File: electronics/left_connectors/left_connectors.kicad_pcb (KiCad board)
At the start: 2 copper layers, 47.5 x 41.3 mm, 0 parts

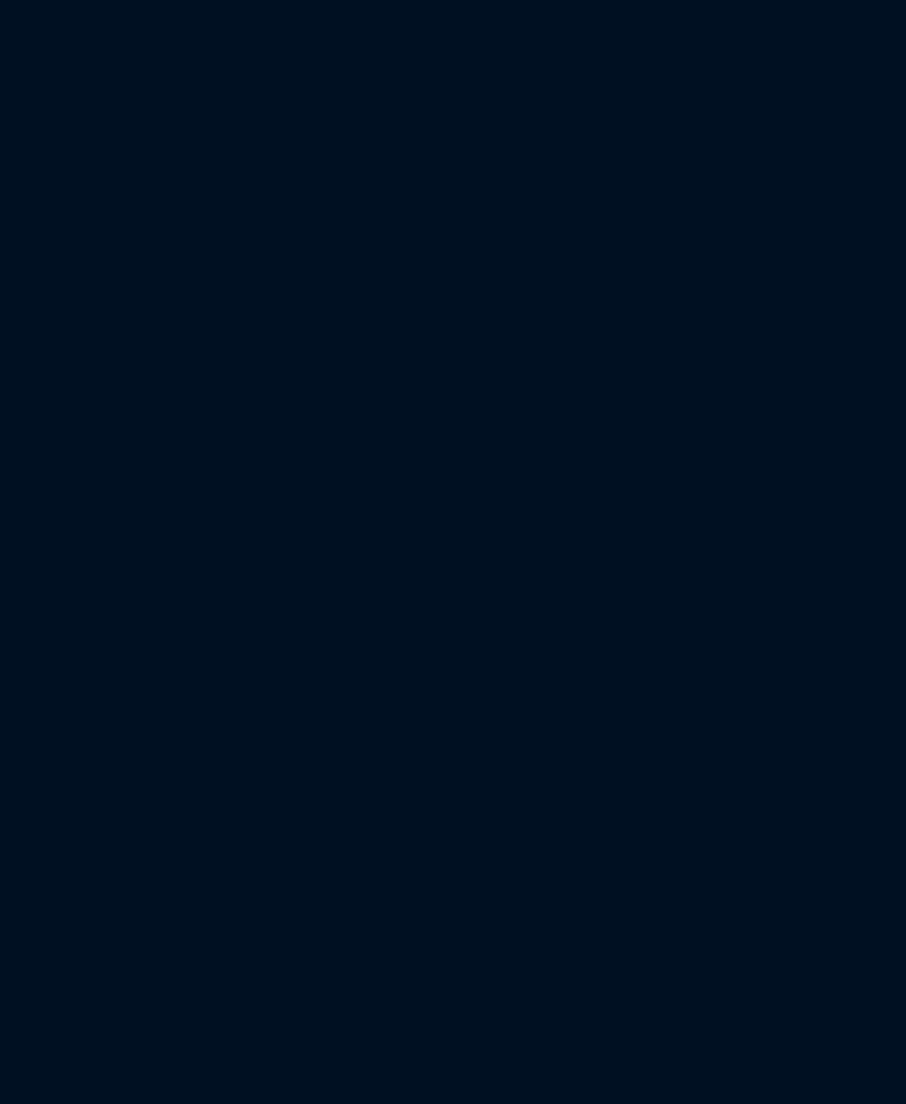
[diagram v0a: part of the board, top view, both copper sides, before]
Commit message: connectors board parts allocated
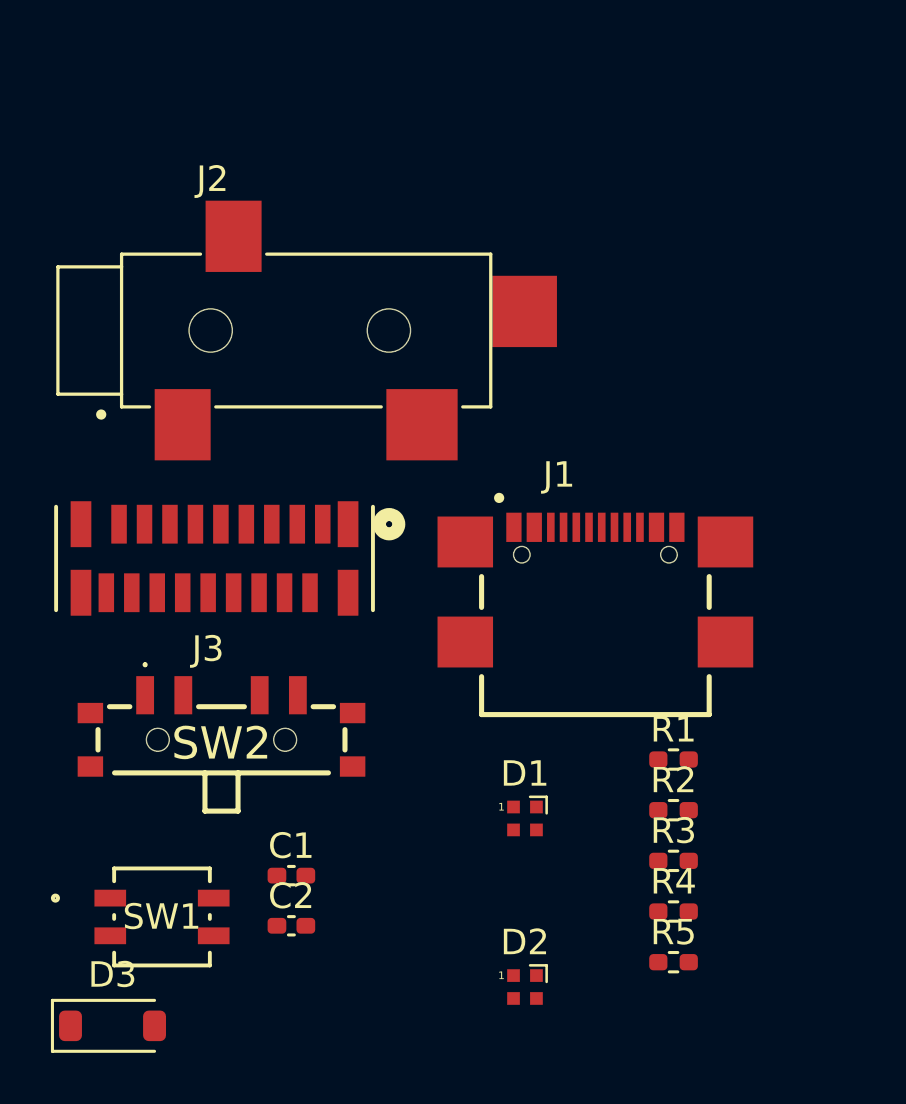
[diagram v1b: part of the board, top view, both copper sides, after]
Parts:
- added C1: 1uF, Capacitor_SMD:C_0402_1005Metric_Pad0.74x0.62mm_HandSolder, F.Cu at (100.8, 148.5)
- added C2: 1uF, Capacitor_SMD:C_0402_1005Metric_Pad0.74x0.62mm_HandSolder, F.Cu at (100.8, 150.5)
- added D1: power_led, LED_SMD:LED_SK6812_EC15_1.5x1.5mm, F.Cu at (110.0, 146.3)
- added D2: ANC_led, LED_SMD:LED_SK6812_EC15_1.5x1.5mm, F.Cu at (110.0, 152.9)
- added D3: MBR120, Diode_SMD:D_SOD-123, F.Cu at (93.8, 154.4)
- added J1: USB_C_Receptacle_USB2.0, USB4110-GF-A_REVB:GCT_USB4110-GF-A_REVB, F.Cu at (112.7, 135.9)
- added J2: Audio In, SJ-3524-SMT:CUI_SJ-3524-SMT, F.Cu at (97.6, 127.1)
- added J3: Main board, FH12-18S-0.5SVA(54):CON18_1X18_DUTB_HRS_HIR, F.Cu at (97.8, 136.0)
- added R1: 1M, Resistor_SMD:R_0402_1005Metric_Pad0.72x0.64mm_HandSolder, F.Cu at (115.8, 143.9)
- added R2: 5.1K, Resistor_SMD:R_0402_1005Metric_Pad0.72x0.64mm_HandSolder, F.Cu at (115.8, 145.9)
- added R3: 5.1K, Resistor_SMD:R_0402_1005Metric_Pad0.72x0.64mm_HandSolder, F.Cu at (115.8, 147.9)
- added R4: 10k, Resistor_SMD:R_0402_1005Metric_Pad0.72x0.64mm_HandSolder, F.Cu at (115.8, 149.9)
- added R5: 50k, Resistor_SMD:R_0402_1005Metric_Pad0.72x0.64mm_HandSolder, F.Cu at (115.8, 151.9)
- added SW1: Power, ul_EVQ-P7A01P:EVQ_P7_PAN, F.Cu at (95.7, 150.1)
- added SW2: ANC_control, CUS-13TB:CUS13B, F.Cu at (98.0, 143.2)

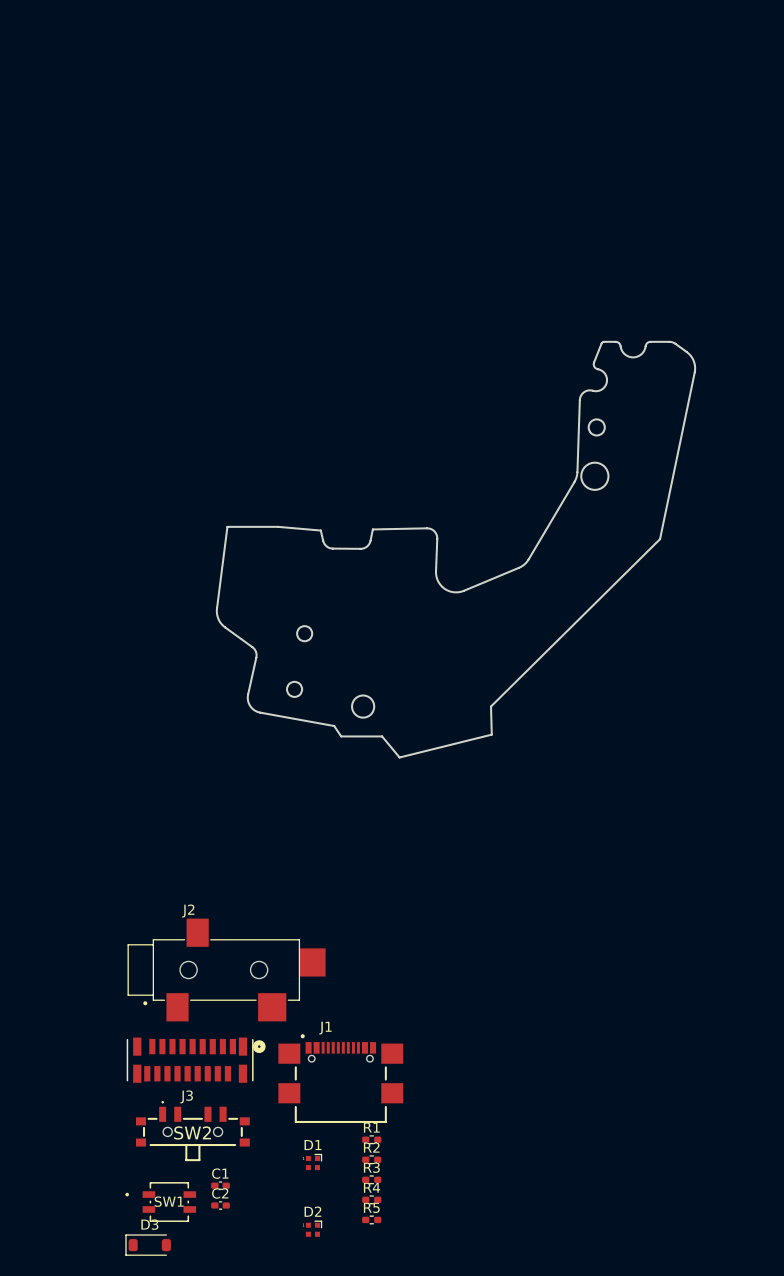
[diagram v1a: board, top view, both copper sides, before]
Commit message: pcbs done, filters need to be finalised
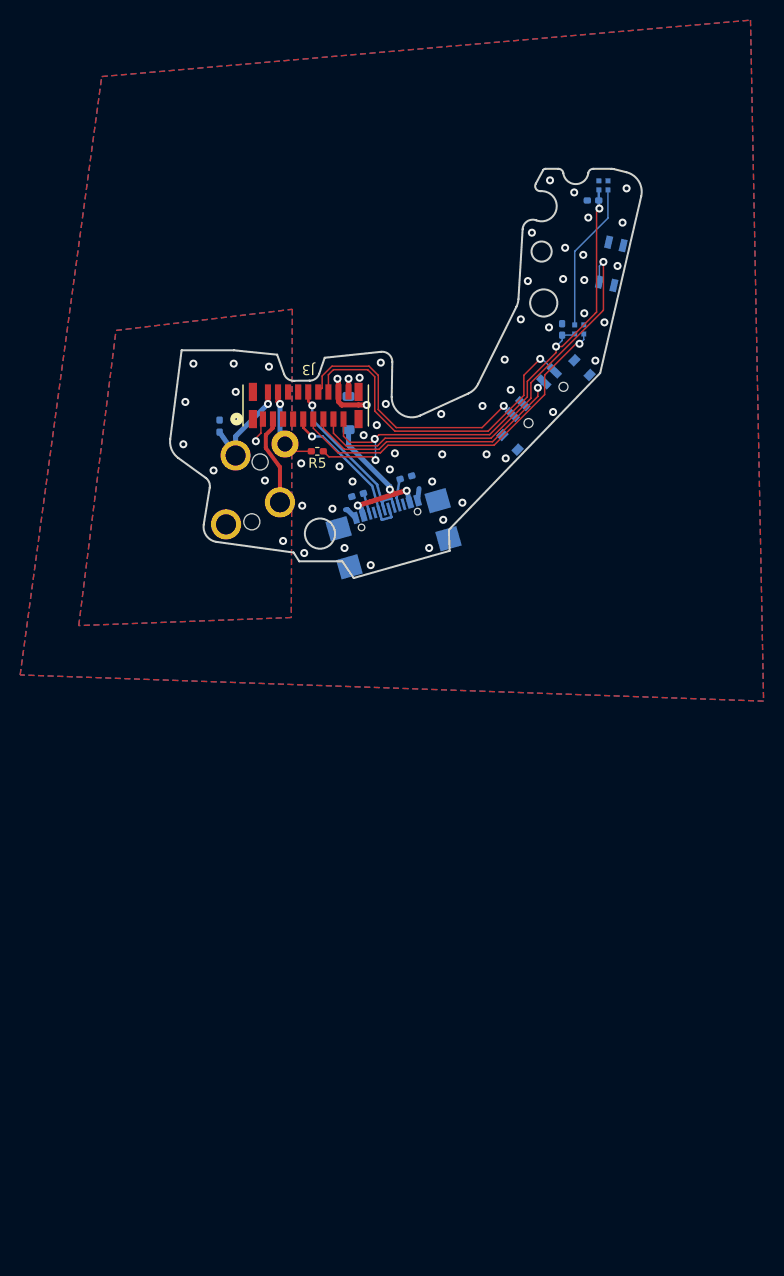
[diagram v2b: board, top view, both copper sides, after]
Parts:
- removed R1: 1M, Resistor_SMD:R_0402_1005Metric_Pad0.72x0.64mm_HandSolder
- C1, C2, D1, D2, D3, J1, R2, R3, R4, SW1, SW2: moved to B.Cu
- J2: footprint SJ-3524-SMT:CUI_SJ-3524-SMT -> SCHURTER Inc 4832.2330:4832.2330; moved to B.Cu
- moved D2 107.6 mm to (138.8, 49.2), turned to 180 degrees
- moved C2 106.4 mm to (137.8, 50.7), turned to 180 degrees
- moved SW1 103.0 mm to (139.6, 57.0), turned to 76.926 degrees
- moved C1 91.5 mm to (134.7, 63.5), turned to 90 degrees
- moved D1 86.9 mm to (136.4, 63.5), turned to 180 degrees
- moved D3 84.9 mm to (113.5, 71.8), turned to -90 degrees
- moved SW2 80.2 mm to (133.1, 71.0), turned to -133.978 degrees
- moved R4 78.3 mm to (100.7, 73.1), turned to 90 degrees
- moved R5 76.5 mm to (110.4, 75.6), turned to 180 degrees
- moved R3 69.8 mm to (119.2, 78.2), turned to 15.811 degrees
- moved R2 66.0 mm to (114.4, 79.9), turned to -164.189 degrees
- moved J3 66.0 mm to (109.2, 71.1), turned to 180 degrees
- moved J1 53.7 mm to (117.6, 82.4), turned to -164.189 degrees
- moved J2 44.3 mm to (103.8, 83.2), turned to 172.125 degrees
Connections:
- J1 pad S1: Net-(J1-SHIELD) -> GND
- J3 pad 20: GND -> GNDA
- J3 pad 21: (no net) -> GND
- J3 pad 22: (no net) -> GNDA
- SW2 pad MP1: (no net) -> GND
- SW2 pad MP2: (no net) -> GND
- SW2 pad MP3: (no net) -> GND
- SW2 pad MP4: (no net) -> GND
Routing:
- net +3V3: track 0.00 -> 56.3 mm, vias 0 -> 4
- net /PWR_SW: track 0.00 -> 42.2 mm, vias 0 -> 1
- net /LEDs_data_in: track 0.00 -> 35.1 mm, vias 0 -> 1
- net /ANC_ON: track 0.00 -> 33.5 mm, vias 0 -> 1
- net /ANC_OFF: track 0.00 -> 26.9 mm, vias 0 -> 1
- net /ANC_PBO: track 0.00 -> 26.8 mm, vias 0 -> 1
- net /USB_D-: track 0.00 -> 16.8 mm, vias 0 -> 1
- net Net-(D3-A): track 0.00 -> 16.0 mm, vias 0 -> 3
- net /USB_D+: track 0.00 -> 15.5 mm, vias 0 -> 1
- net Net-(D1-DOUT): track 0.00 -> 14.8 mm
- net /audio_in_L: track 0.00 -> 10.5 mm, vias 0 -> 1
- net /audio_in_R: track 0.00 -> 9.01 mm
- net /audio_in_detect: track 0.00 -> 8.37 mm, vias 0 -> 1
- net GND: track 0.00 -> 7.76 mm, vias 0 -> 46
- net VBUS: track 0.00 -> 3.06 mm, vias 0 -> 1
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- added copper zone on B.Cu, net GND
- added copper zone on F.Cu, net GND
- added copper zone on B.Cu, net GNDA
- added copper zone on F.Cu, net GNDA
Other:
- board size 47.5 x 41.3 mm -> 46.8 x 40.6 mm
